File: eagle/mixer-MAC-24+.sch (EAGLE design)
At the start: 10 parts, among them U1 MAC-24+, X1 SMA, X2 SMA, X3 SMA

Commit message: Gnd fix
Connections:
- net GND: now also X1.2, X2.2
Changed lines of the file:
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@@
 <part name="R2" library="oresat-rcl" deviceset="R-US_" device="0402-B-NOSILK" value="0"/>
 <part name="R3" library="oresat-rcl" deviceset="R-US_" device="0402-B-NOSILK" value="0"/>
+<part name="GND3" library="supply1" library_urn="urn:adsk.eagle:library:371" deviceset="GND" device=""/>
+<part name="GND4" library="supply1" library_urn="urn:adsk.eagle:library:371" deviceset="GND" device=""/>
 </parts>
 <sheets>
@@
 <attribute name="VALUE" x="140.97" y="118.618" size="1.778" layer="96"/>
 </instance>
+<instance part="GND3" gate="1" x="78.74" y="124.46" smashed="yes">
+<attribute name="VALUE" x="76.2" y="121.92" size="1.778" layer="96"/>
+</instance>
+<instance part="GND4" gate="1" x="78.74" y="96.52" smashed="yes">
+<attribute name="VALUE" x="76.2" y="93.98" size="1.778" layer="96"/>
+</instance>
 </instances>
 <busses>
@@
 <pinref part="GND2" gate="1" pin="GND"/>
 </segment>
+<segment>
+<pinref part="GND4" gate="1" pin="GND"/>
+<pinref part="X2" gate="G1" pin="2"/>
+<wire x1="78.74" y1="99.06" x2="78.74" y2="101.6" width="0.1524" layer="91"/>
+</segment>
+<segment>
+<pinref part="GND3" gate="1" pin="GND"/>
+<pinref part="X1" gate="G1" pin="2"/>
+<wire x1="78.74" y1="127" x2="78.74" y2="129.54" width="0.1524" layer="91"/>
+</segment>
 </net>

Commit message: Add initial layout
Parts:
- removed X1, X2, X3: SMA, con-coax:SMA-142-0701-801/806
- added J1, J2, J3: 142-0701-851, J-Cinch-142-0701-851-SMA-end-launch:142-0701-851
- AT1, AT2: value 2dB -> (none)
- AT3: value 3dB -> (none)
- R1, R2, R3: device oresat-rcl:R-US_0402-B-NOSILK -> oresat-rcl:R-US_0402-C-NOSILK
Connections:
- removed net N$2: AT2.2, X3.1
- removed net N$3: AT1.1, X1.1
- removed net N$5: AT3.1, X2.1
- new net IF: AT3.2, J3.RF
- new net LO: AT2.1, J2.RF
- new net RF: AT1.1, J1.RF
- net GND: now also J1.GND, J2.GND, J3.GND; no longer X1.2, X2.2, X3.2
- net N$4: now also R1.2; no longer R2.2
- net N$6: now also R2.2; no longer R1.2
- net N$7: now also AT2.2, R2.1; no longer AT3.2, R1.1
- net N$8: now also R1.1; no longer R2.1
- net N$9: now also AT3.1; no longer AT2.1
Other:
- note added: "Attenuators: Susumu PAT1220 0805 - 100mW Short w/ 0402"
- note removed: "Attenuators: Susumu PAT1220 0805 - 100mW"
- moved on the sheet: AT2, AT3, R1, R2

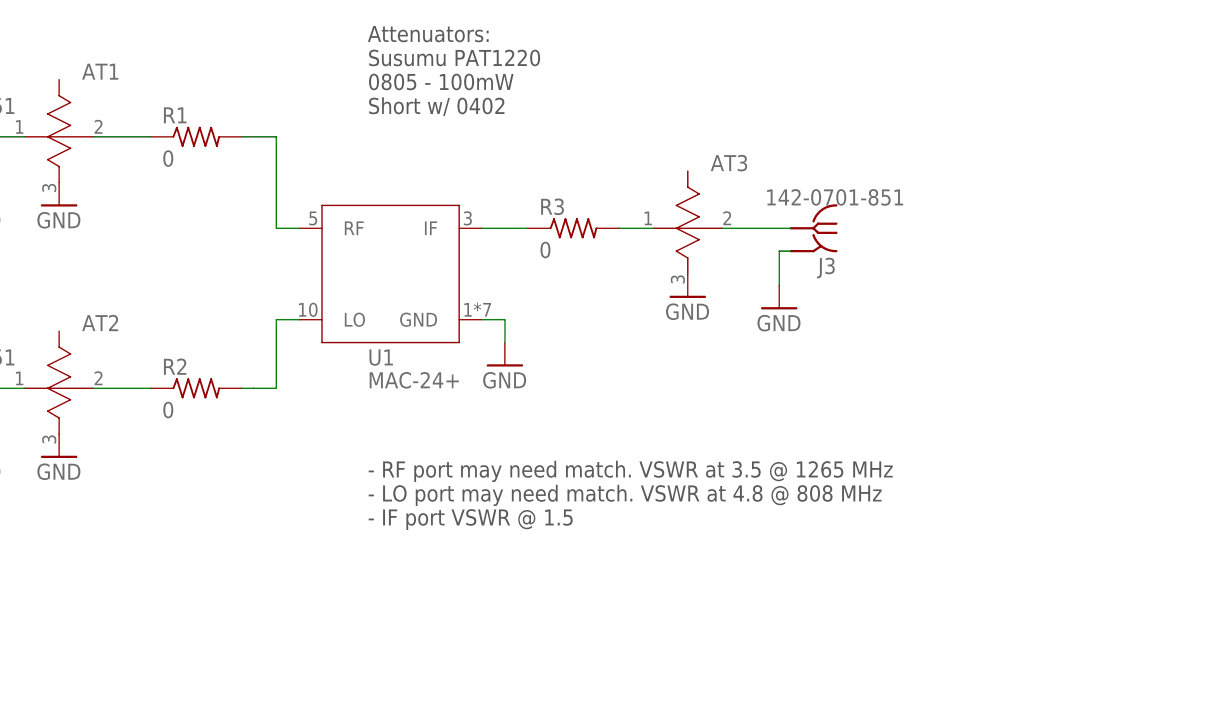
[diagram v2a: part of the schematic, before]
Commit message: Add stitching and finalize
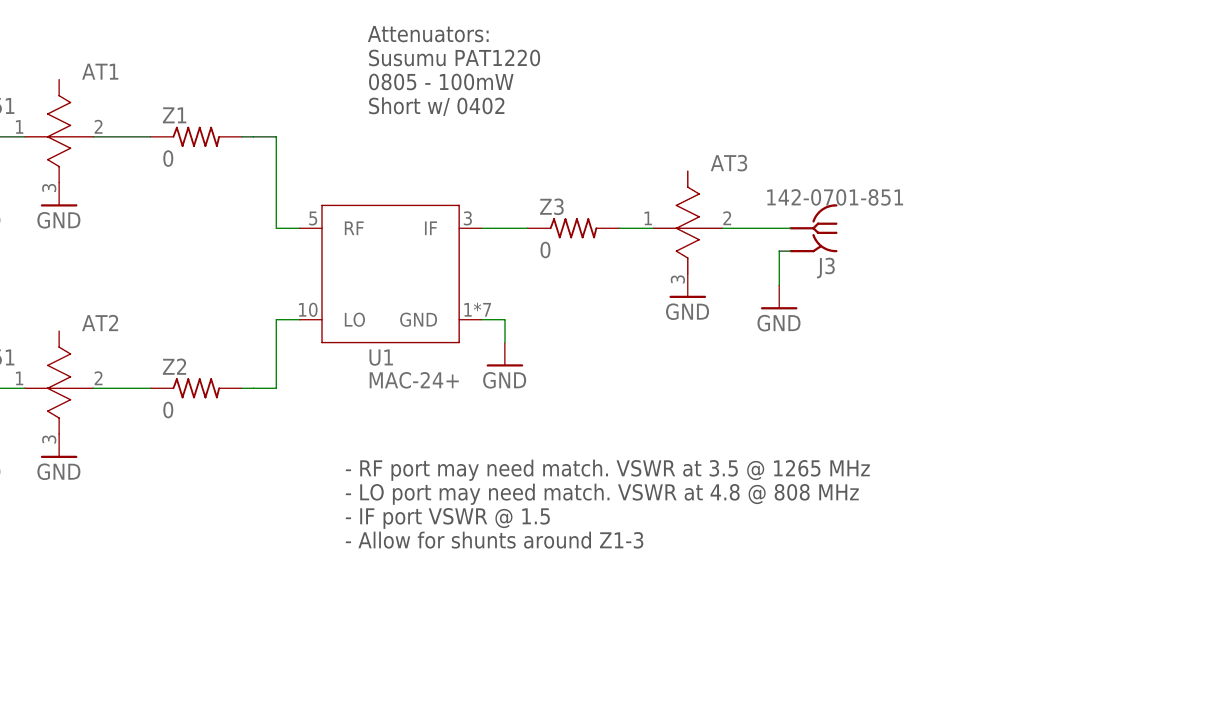
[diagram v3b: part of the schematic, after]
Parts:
- renumbered R1 to Z1, R2 to Z2, R3 to Z3
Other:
- note added: "- RF port may need match. VSWR at 3.5 @ 1265 MHz - LO port may need match. VSWR at 4.8 @ 808 MHz - IF port VSWR @ 1.5 - Allow for shunts around Z1-3"
- note removed: "- RF port may need match. VSWR at 3.5 @ 1265 MHz - LO port may need match. VSWR at 4.8 @ 808 MHz - IF port VSWR @ 1.5"
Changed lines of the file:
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@@
 <part name="GND2" library="supply1" library_urn="urn:adsk.eagle:library:371" deviceset="GND" device=""/>
 <part name="AT2" library="AT-Susumu-PAT-attenuator" deviceset="PAT1220" device=""/>
-<part name="R2" library="oresat-rcl" deviceset="R-US_" device="0402-C-NOSILK" value="0"/>
-<part name="R1" library="oresat-rcl" deviceset="R-US_" device="0402-C-NOSILK" value="0"/>
-<part name="R3" library="oresat-rcl" deviceset="R-US_" device="0402-C-NOSILK" value="0"/>
+<part name="Z2" library="oresat-rcl" deviceset="R-US_" device="0402-C-NOSILK" value="0"/>
+<part name="Z1" library="oresat-rcl" deviceset="R-US_" device="0402-C-NOSILK" value="0"/>
+<part name="Z3" library="oresat-rcl" deviceset="R-US_" device="0402-C-NOSILK" value="0"/>
 <part name="GND3" library="supply1" library_urn="urn:adsk.eagle:library:371" deviceset="GND" device=""/>
 <part name="GND4" library="supply1" library_urn="urn:adsk.eagle:library:371" deviceset="GND" device=""/>
@@
 <text x="176.53" y="26.67" size="5.08" layer="94">Mixer: MiniCirc.Mac-24+</text>
 <text x="265.43" y="6.35" size="3.81" layer="94">1</text>
-<text x="121.92" y="88.9" size="1.778" layer="97">- RF port may need match. VSWR at 3.5 @ 1265 MHz
+<text x="119.38" y="86.36" size="1.778" layer="97">- RF port may need match. VSWR at 3.5 @ 1265 MHz
 - LO port may need match. VSWR at 4.8 @ 808 MHz
-- IF port VSWR @ 1.5</text>
+- IF port VSWR @ 1.5
+- Allow for shunts around Z1-3</text>
 <text x="121.92" y="134.62" size="1.778" layer="97">Attenuators:
 Susumu PAT1220
@@
 <attribute name="VALUE" x="90.17" y="107.95" size="1.778" layer="96"/>
 </instance>
-<instance part="R2" gate="R" x="102.87" y="104.14" smashed="yes">
+<instance part="Z2" gate="R" x="102.87" y="104.14" smashed="yes">
 <attribute name="NAME" x="99.06" y="105.6386" size="1.778" layer="95"/>
 <attribute name="VALUE" x="99.06" y="100.838" size="1.778" layer="96"/>
 </instance>
-<instance part="R1" gate="R" x="102.87" y="132.08" smashed="yes">
+<instance part="Z1" gate="R" x="102.87" y="132.08" smashed="yes">
 <attribute name="NAME" x="99.06" y="133.5786" size="1.778" layer="95"/>
 <attribute name="VALUE" x="99.06" y="128.778" size="1.778" layer="96"/>
 </instance>
-<instance part="R3" gate="R" x="144.78" y="121.92" smashed="yes">
+<instance part="Z3" gate="R" x="144.78" y="121.92" smashed="yes">
 <attribute name="NAME" x="140.97" y="123.4186" size="1.778" layer="95"/>
 <attribute name="VALUE" x="140.97" y="118.618" size="1.778" layer="96"/>
@@
 <pinref part="U1" gate="G$1" pin="RF"/>
 <wire x1="111.76" y1="121.92" x2="114.3" y2="121.92" width="0.1524" layer="91"/>
-<pinref part="R1" gate="R" pin="2"/>
-<wire x1="107.95" y1="132.08" x2="111.76" y2="132.08" width="0.1524" layer="91"/>
+<pinref part="Z1" gate="R" pin="2"/>
+<wire x1="107.95" y1="132.08" x2="109.22" y2="132.08" width="0.1524" layer="91"/>
+<wire x1="109.22" y1="132.08" x2="111.76" y2="132.08" width="0.1524" layer="91"/>
 </segment>
 </net>
@@
 <wire x1="111.76" y1="104.14" x2="111.76" y2="111.76" width="0.1524" layer="91"/>
 <wire x1="111.76" y1="111.76" x2="114.3" y2="111.76" width="0.1524" layer="91"/>
-<pinref part="R2" gate="R" pin="2"/>
+<pinref part="Z2" gate="R" pin="2"/>
 <wire x1="111.76" y1="104.14" x2="109.22" y2="104.14" width="0.1524" layer="91"/>
 <wire x1="109.22" y1="104.14" x2="107.95" y2="104.14" width="0.1524" layer="91"/>
@@
 <segment>
 <pinref part="AT2" gate="G$1" pin="2"/>
-<pinref part="R2" gate="R" pin="1"/>
+<pinref part="Z2" gate="R" pin="1"/>
 <wire x1="91.44" y1="104.14" x2="97.79" y2="104.14" width="0.1524" layer="91"/>
 </segment>
@@
 <segment>
 <pinref part="AT1" gate="G$1" pin="2"/>
-<pinref part="R1" gate="R" pin="1"/>
+<pinref part="Z1" gate="R" pin="1"/>
 <wire x1="91.44" y1="132.08" x2="97.79" y2="132.08" width="0.1524" layer="91"/>
 </segment>
@@
 <segment>
 <pinref part="U1" gate="G$1" pin="IF"/>
-<pinref part="R3" gate="R" pin="1"/>
+<pinref part="Z3" gate="R" pin="1"/>
 <wire x1="134.62" y1="121.92" x2="139.7" y2="121.92" width="0.1524" layer="91"/>
 </segment>
@@
 <net name="N$9" class="1">
 <segment>
-<pinref part="R3" gate="R" pin="2"/>
+<pinref part="Z3" gate="R" pin="2"/>
 <pinref part="AT3" gate="G$1" pin="1"/>
 <wire x1="149.86" y1="121.92" x2="153.67" y2="121.92" width="0.1524" layer="91"/>
@@
 </sheet>
 </sheets>
+<errors>
+</errors>
 </schematic>
 </drawing>
